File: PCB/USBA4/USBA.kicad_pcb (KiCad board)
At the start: 2 copper layers, 70 x 70 mm, 23 parts, among them J1 USB_A, J2 Shelly, U2 ESP32-S3-MINI-1, U5 MD8942, U6 SHT40

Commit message: Fix cuts
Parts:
- moved PCB1 7.51 mm to (100.0, 100.0)
- moved C2 4.51 mm to (107.1, 105.0)
- moved C3 4.51 mm to (106.7, 103.5)
- moved C6 4.51 mm to (107.2, 97.3)
- moved C7 4.51 mm to (102.2, 97.3)
- moved C8 4.51 mm to (104.7, 96.6)
- moved J1 4.51 mm to (121.0, 99.3)
- moved J2 4.51 mm to (108.9, 99.3)
- moved L2 4.51 mm to (104.7, 94.0)
- moved R1 4.51 mm to (106.2, 105.0)
- moved R5 4.51 mm to (102.2, 105.3)
- moved R7 4.51 mm to (102.2, 103.5)
- moved R9 4.51 mm to (104.7, 100.5)
- moved U2 4.51 mm to (93.4, 99.3)
- moved U5 4.51 mm to (104.7, 98.6)
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
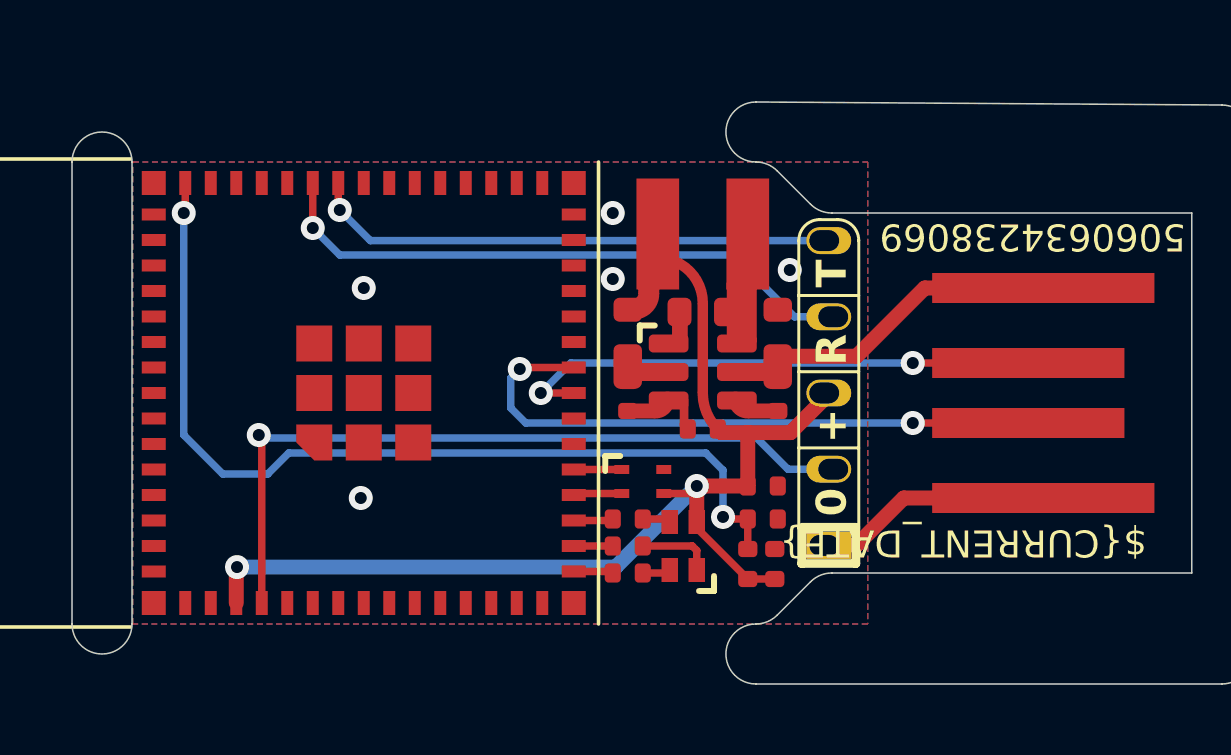
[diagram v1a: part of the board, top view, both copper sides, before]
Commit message: Tidy, fix GND, and add tear drops
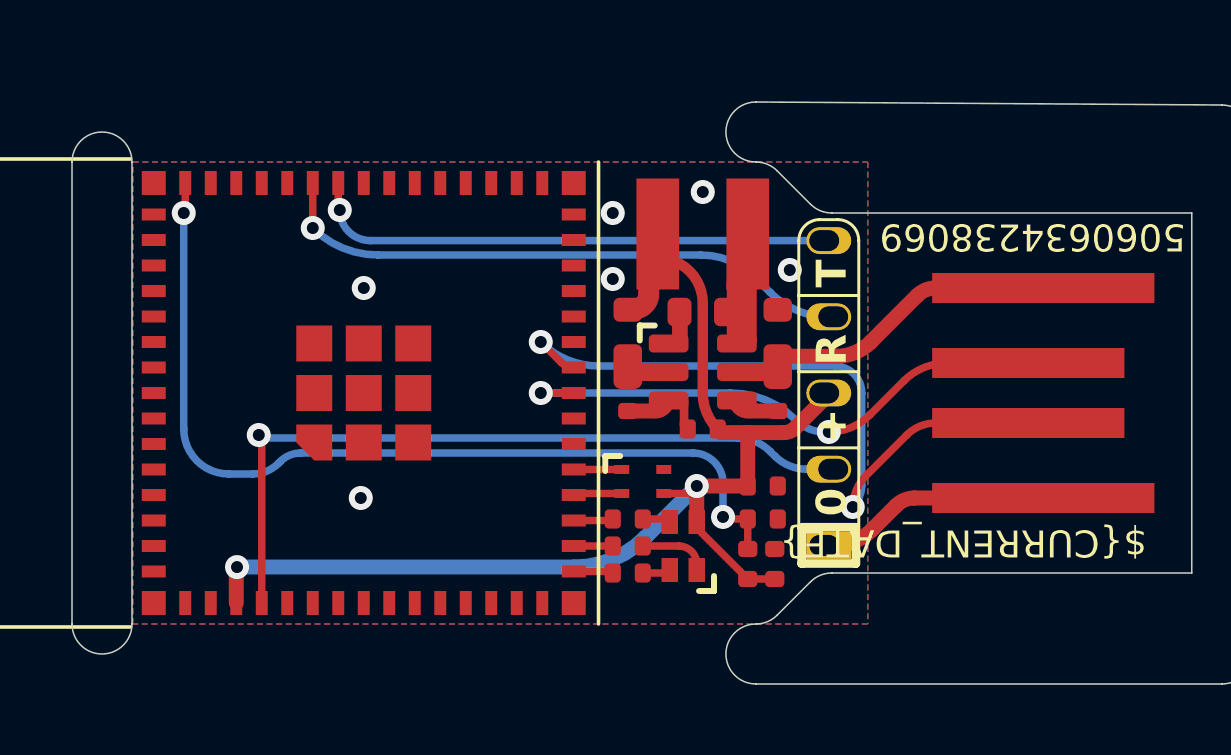
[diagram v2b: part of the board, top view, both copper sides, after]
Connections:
- U2 pad 59: (no net) -> GND
- U2 pad 62: (no net) -> GND
- U2 pad 63: (no net) -> GND
- U2 pad 64: (no net) -> GND
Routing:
- net D+: track 20.7 -> 23.9 mm
- net D-: track 17.8 -> 15.7 mm
- net Net-(J2-Rx): track 20.1 -> 19.5 mm
- net GND: track 7.95 -> 7.51 mm, vias 5 -> 6

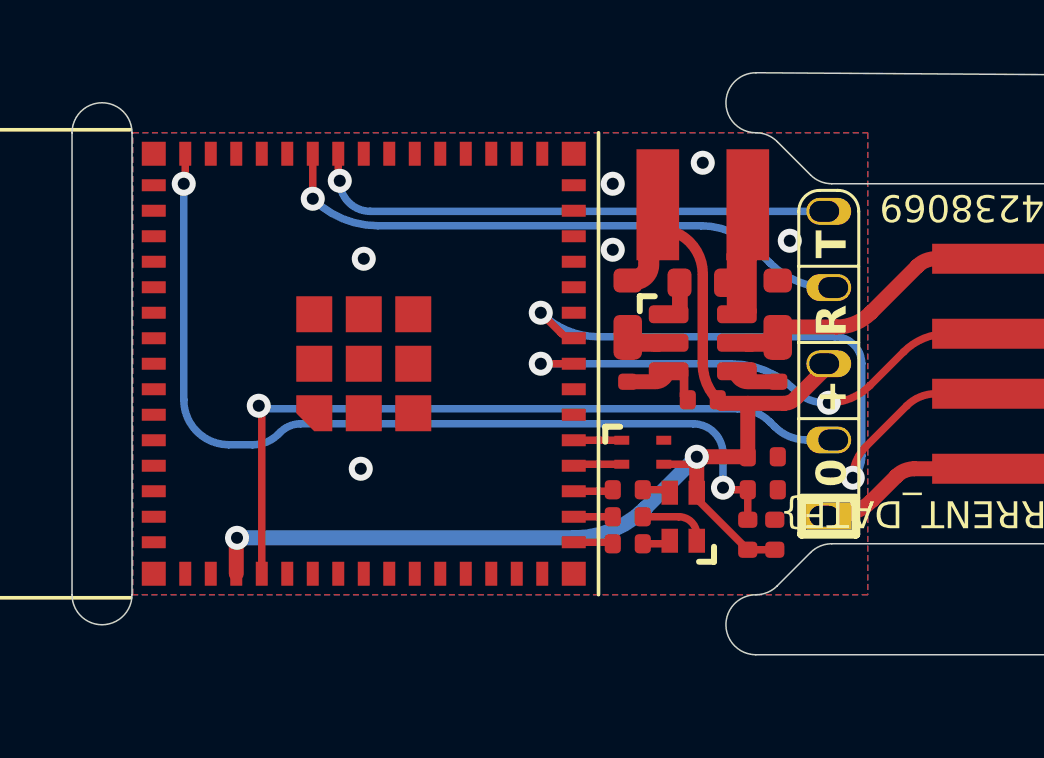
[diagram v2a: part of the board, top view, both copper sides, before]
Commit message: PROG under ESP
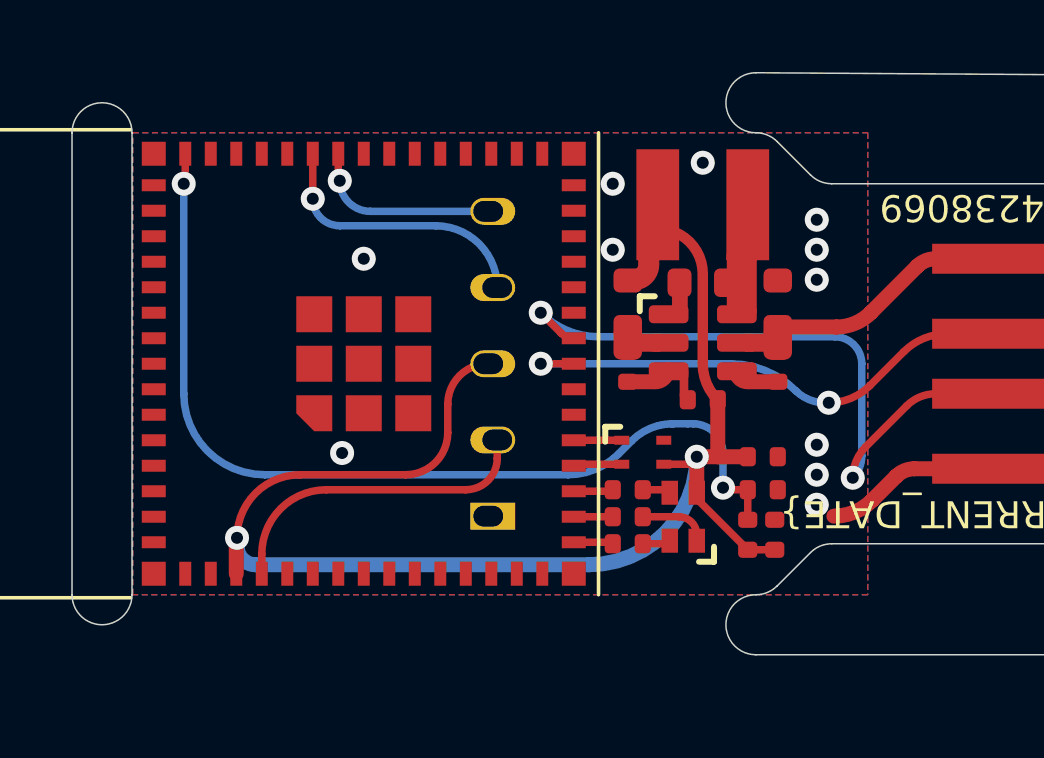
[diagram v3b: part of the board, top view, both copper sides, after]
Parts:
- moved J2 11.2 mm to (97.7, 99.3)
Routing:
- net Net-(J2-0): track 25.1 -> 10.8 mm, vias 1 -> 0
- net Net-(J2-Tx): track 17.6 -> 6.41 mm
- net Net-(J2-Rx): track 19.5 -> 9.22 mm
- net +3.3V: track 30.7 -> 40.3 mm
- net Net-(U2-EN): track 30.7 -> 31.5 mm
- net GND: vias 6 -> 11

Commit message: SMaller
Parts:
- moved C6 1.09 mm to (106.9, 98.3)
- moved C7 1.09 mm to (101.9, 98.3)
- moved C8 1.09 mm to (104.4, 97.6)
- moved L2 1.09 mm to (104.4, 95.0)
- moved R9 1.09 mm to (104.4, 101.5)
- moved U5 1.09 mm to (104.4, 99.6)
- moved R10 1.09 mm to (101.9, 100.4)
- moved R11 1.09 mm to (106.9, 100.4)
- moved J1 1.00 mm to (120.0, 99.3)
- moved R5 0.98 mm to (102.6, 106.2)
- moved R7 0.98 mm to (102.6, 104.4)
- moved D2 0.98 mm to (104.5, 105.3)
- moved R4 0.98 mm to (102.6, 105.3)
- moved U6 0.75 mm to (102.7, 103.0)
- moved C1 0.50 mm to (106.7, 101.9)
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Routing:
- net +3.3V: track 40.3 -> 37.9 mm
- net D+: track 23.9 -> 25.7 mm
- net D-: track 15.7 -> 16.6 mm
- net G: track 1.25 -> 2.01 mm
- net B: track 1.25 -> 1.98 mm
- net R: track 1.30 -> 2.01 mm
- net GND: track 7.51 -> 8.15 mm, vias 11 -> 10
